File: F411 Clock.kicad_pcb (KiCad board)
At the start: 2 copper layers, 2 parts, among them U1 STM32F411CCUx

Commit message: PCB Save: 1 files changed F411 Clock.kicad_pcb 644/0/0
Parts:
- added J1: USB_C_Receptacle_USB2.0_16P, Connector_USB:USB_C_Receptacle_HCTL_HC-TYPE-C-16P-01A, F.Cu at (108.3, 87.4)
- added R1: R_Small, Resistor_SMD:R_0805_2012Metric, F.Cu at (104.5, 96.0)

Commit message: PCB Save: 1 files changed F411 Clock.kicad_pcb 0/0/2
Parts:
- moved J1 5.73 mm to (106.5, 82.0)
- moved U1 5.73 mm to (124.2, 80.7)
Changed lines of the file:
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@@
 	(footprint "Connector_USB:USB_C_Receptacle_HCTL_HC-TYPE-C-16P-01A"
 		(layer "F.Cu")
-		(at 108.345 87.425)
+		(at 106.5 82)
 		(descr "16-pin USB-C receptacle, USB2.0 and PD, 5A VBUS rating, https://datasheet.lcsc.com/lcsc/2211161000_HCTL-HC-TYPE-C-16P-01A_C2894897.pdf")
 		(tags "usb usb-c 2.0 pd")
@@
 	(footprint "Package_DFN_QFN:QFN-48-1EP_7x7mm_P0.5mm_EP5.15x5.15mm"
 		(layer "F.Cu")
-		(at 126.065 86.145)
+		(at 124.22 80.72)
 		(descr "QFN, 48 Pin (http://www.analog.com/media/en/package-pcb-resources/package/pkg_pdf/ltc-legacy-qfn/QFN_48_05-08-1704.pdf)")
 		(tags "QFN NoLead")

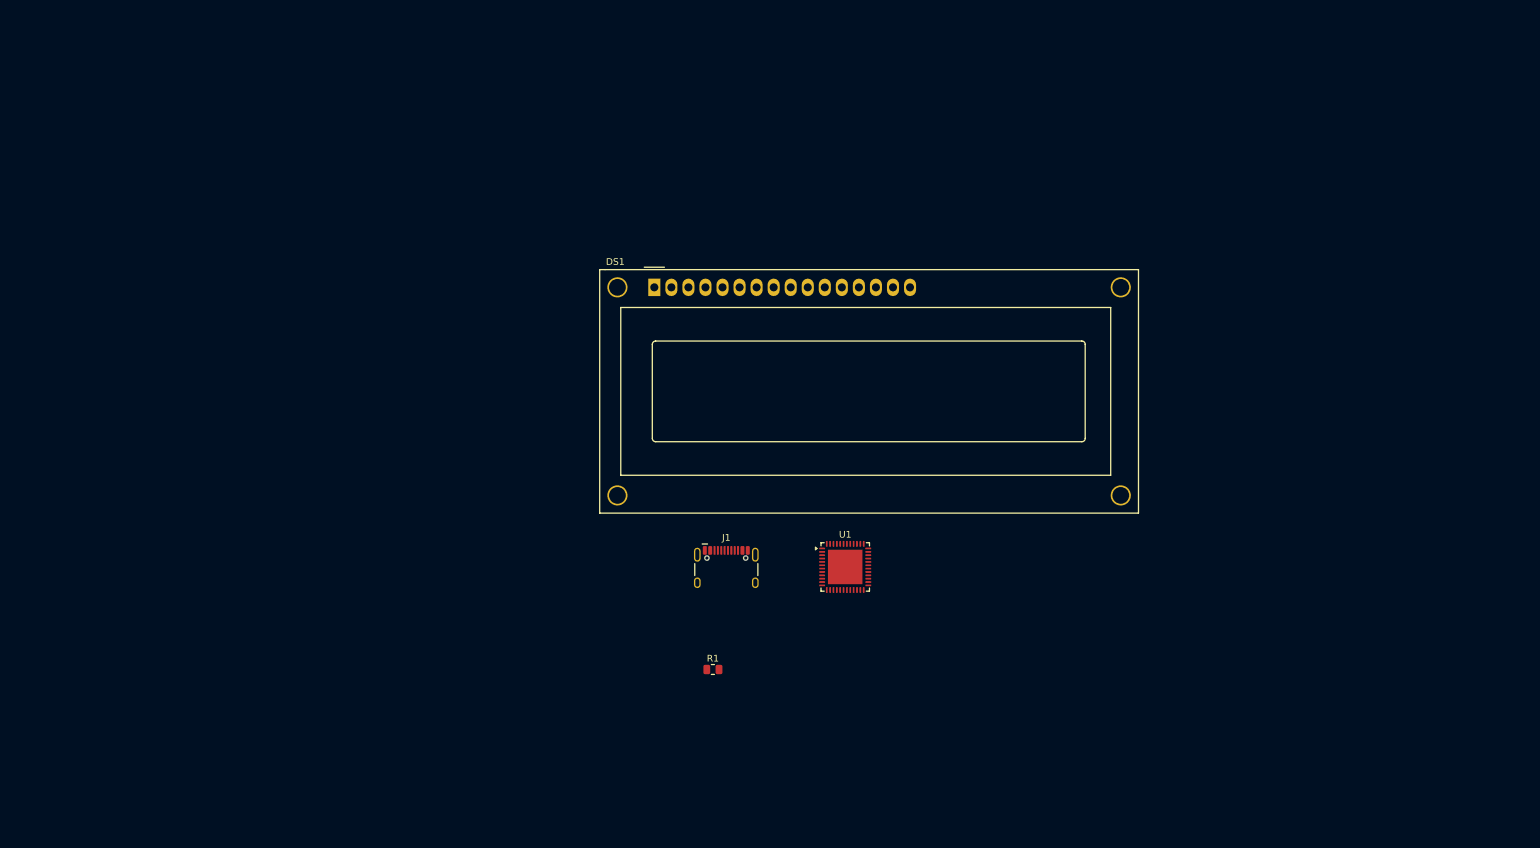
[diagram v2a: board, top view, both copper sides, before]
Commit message: Add .gitignore and update PCB footprints; remove unused files
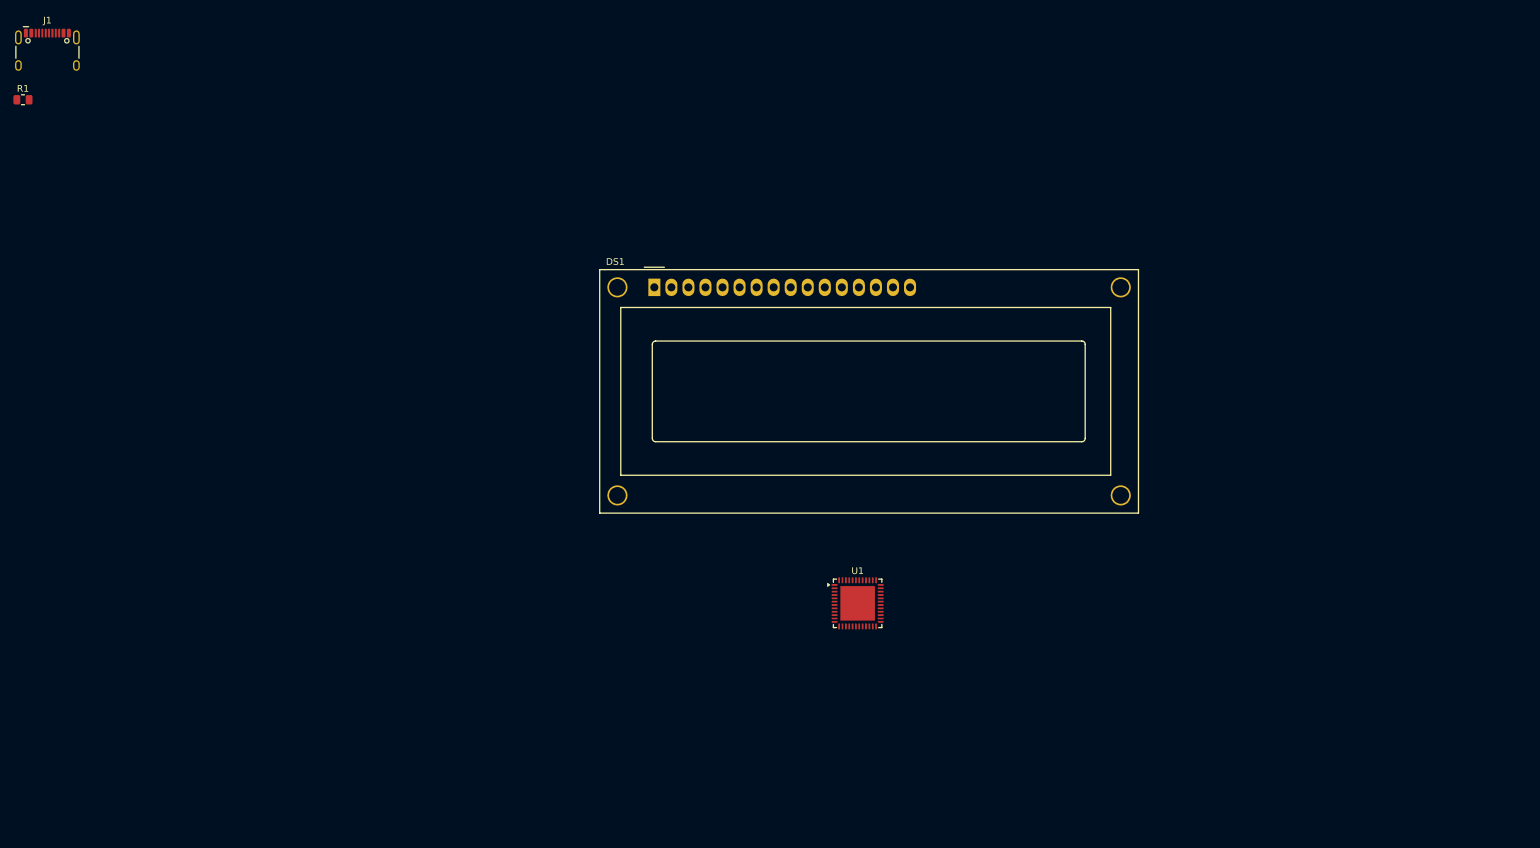
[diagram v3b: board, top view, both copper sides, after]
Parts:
- moved R1 133.3 mm to (1.71, 11.1)
- moved J1 127.2 mm to (5.34, 4.92)
- moved U1 5.73 mm to (126.1, 86.1)
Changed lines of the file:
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@@
 	(footprint "Connector_USB:USB_C_Receptacle_HCTL_HC-TYPE-C-16P-01A"
 		(layer "F.Cu")
-		(at 106.5 82)
+		(at 5.345 4.925)
 		(descr "16-pin USB-C receptacle, USB2.0 and PD, 5A VBUS rating, https://datasheet.lcsc.com/lcsc/2211161000_HCTL-HC-TYPE-C-16P-01A_C2894897.pdf")
 		(tags "usb usb-c 2.0 pd")
@@
 	(footprint "Resistor_SMD:R_0805_2012Metric"
 		(layer "F.Cu")
-		(at 104.5 96)
+		(at 1.705 11.105)
 		(descr "Resistor SMD 0805 (2012 Metric), square (rectangular) end terminal, IPC-7351 nominal, (Body size source: IPC-SM-782 page 72, https://www.pcb-3d.com/wordpress/wp-content/uploads/ipc-sm-782a_amendment_1_and_2.pdf)")
 		(tags "resistor")
@@
 	(footprint "Package_DFN_QFN:QFN-48-1EP_7x7mm_P0.5mm_EP5.15x5.15mm"
 		(layer "F.Cu")
-		(at 124.22 80.72)
+		(at 126.065 86.145)
 		(descr "QFN, 48 Pin (http://www.analog.com/media/en/package-pcb-resources/package/pkg_pdf/ltc-legacy-qfn/QFN_48_05-08-1704.pdf)")
 		(tags "QFN NoLead")

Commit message: Close: 3 files changed F411 Clock.kicad_pcb 0/0/3 F411 Clock.kicad_prl 138/0/0 F411 Clock.kicad_pro 651/0/0
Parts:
- moved R1 133.3 mm to (104.5, 96.0)
- moved J1 127.2 mm to (106.5, 82.0)
- moved U1 5.73 mm to (124.2, 80.7)
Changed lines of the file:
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@@
 	(footprint "Connector_USB:USB_C_Receptacle_HCTL_HC-TYPE-C-16P-01A"
 		(layer "F.Cu")
-		(at 5.345 4.925)
+		(at 106.5 82)
 		(descr "16-pin USB-C receptacle, USB2.0 and PD, 5A VBUS rating, https://datasheet.lcsc.com/lcsc/2211161000_HCTL-HC-TYPE-C-16P-01A_C2894897.pdf")
 		(tags "usb usb-c 2.0 pd")
@@
 	(footprint "Resistor_SMD:R_0805_2012Metric"
 		(layer "F.Cu")
-		(at 1.705 11.105)
+		(at 104.5 96)
 		(descr "Resistor SMD 0805 (2012 Metric), square (rectangular) end terminal, IPC-7351 nominal, (Body size source: IPC-SM-782 page 72, https://www.pcb-3d.com/wordpress/wp-content/uploads/ipc-sm-782a_amendment_1_and_2.pdf)")
 		(tags "resistor")
@@
 	(footprint "Package_DFN_QFN:QFN-48-1EP_7x7mm_P0.5mm_EP5.15x5.15mm"
 		(layer "F.Cu")
-		(at 126.065 86.145)
+		(at 124.22 80.72)
 		(descr "QFN, 48 Pin (http://www.analog.com/media/en/package-pcb-resources/package/pkg_pdf/ltc-legacy-qfn/QFN_48_05-08-1704.pdf)")
 		(tags "QFN NoLead")

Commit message: PCB Save: 2 files changed F411 Clock.kicad_pcb 6362/0/1538 ~F411 Clock.kicad_pcb.lck 1/0/0
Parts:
- added BT1: Battery, Battery:BatteryHolder_MPD_BK-18650-PC2, B.Cu at (163.9, 54.0)
- added BT2: Battery_Cell, Battery:BatteryHolder_Keystone_3034_1x20mm, F.Cu at (195.9, 111.1)
- added C1: 10uf, Capacitor_SMD:C_0805_2012Metric, F.Cu at (210.6, 101.5)
- added C2: 10uf, Capacitor_SMD:C_0805_2012Metric, F.Cu at (210.6, 104.5)
- added C3: 10uf, Capacitor_SMD:C_0805_2012Metric, F.Cu at (210.6, 107.6)
- added C4: 10uf, Capacitor_SMD:C_0805_2012Metric, F.Cu at (210.6, 110.6)
- added C5: 10uf, Capacitor_SMD:C_0805_2012Metric, F.Cu at (210.6, 113.6)
- added D1: 1N5819, Diode_SMD:D_0805_2012Metric, F.Cu at (223.9, 106.0)
- added Q1: DMG3415U, Package_TO_SOT_SMD:SOT-23, F.Cu at (224.1, 102.3)
- added Q2: BC547, Package_TO_SOT_THT:TO-92L_Wide, F.Cu at (214.3, 118.9)
- added R10: 10k, Resistor_SMD:R_0805_2012Metric, F.Cu at (219.4, 110.4)
- added R11: 10k, Resistor_SMD:R_0805_2012Metric, F.Cu at (219.4, 113.3)
- added R2: 10k, Resistor_SMD:R_0805_2012Metric, F.Cu at (215.0, 101.5)
- added R3: 5.2k, Resistor_SMD:R_0805_2012Metric, F.Cu at (215.0, 104.5)
- added R4: 5.2k, Resistor_SMD:R_0805_2012Metric, F.Cu at (215.0, 107.4)
- added R5: 10k, Resistor_SMD:R_0805_2012Metric, F.Cu at (215.0, 110.4)
- added R6: 10k, Resistor_SMD:R_0805_2012Metric, F.Cu at (215.0, 113.3)
- added R7: 10k, Resistor_SMD:R_0805_2012Metric, F.Cu at (219.4, 101.5)
- added R8: 10k, Resistor_SMD:R_0805_2012Metric, F.Cu at (219.4, 104.5)
- added R9: 10k, Resistor_SMD:R_0805_2012Metric, F.Cu at (219.4, 107.4)
- added SW1: SW_Push, Button_Switch_SMD:SW_SPST_TL3342, B.Cu at (121.1, 67.5)
- added SW2: SW_Push, Button_Switch_SMD:SW_SPST_TL3342, B.Cu at (114.0, 67.5)
- added SW3: SW_Push, Button_Switch_SMD:SW_SPST_TL3342, B.Cu at (107.0, 67.5)
- added SW4: SW_Push, Button_Switch_SMD:SW_SPST_TL3342, B.Cu at (100.0, 67.5)
- J1: footprint Connector_USB:USB_C_Receptacle_HCTL_HC-TYPE-C-16P-01A -> Connector_USB:USB_C_Receptacle_GCT_USB4105-xx-A_16P_TopMnt_Horizontal
- R1: value R_Small -> 10k
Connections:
- DS1 pad 1: unconnected-(DS1-VSS-Pad1) -> GND
- DS1 pad 15: unconnected-(DS1-LED(+)-Pad15) -> +3.3V
- DS1 pad 16: unconnected-(DS1-LED(-)-Pad16) -> Net-(DS1-LED(-))
- DS1 pad 2: unconnected-(DS1-VDD-Pad2) -> VBUS
- J1 pad A1: Net-(J1-GND-PadA1) -> GND
- J1 pad A12: Net-(J1-GND-PadA1) -> GND
- J1 pad A5: unconnected-(J1-CC1-PadA5) -> Net-(J1-CC1)
- J1 pad B1: Net-(J1-GND-PadA1) -> GND
- J1 pad B12: Net-(J1-GND-PadA1) -> GND
- J1 pad B5: unconnected-(J1-CC2-PadB5) -> Net-(J1-CC2)
- J1 pad SH: unconnected-(J1-SHIELD-PadSH) -> GND
- R1 pad 1: unconnected-(R1-Pad1) -> /DN
- R1 pad 2: unconnected-(R1-Pad2) -> Net-(J1-D--PadA7)
- U1 pad 1: unconnected-(U1-VBAT-Pad1) -> +BATT_2
- U1 pad 23: Net-(U1-VSS-Pad23) -> GND
- U1 pad 24: unconnected-(U1-VDD-Pad24) -> +3.3V
- U1 pad 32: unconnected-(U1-PA11-Pad32) -> /DN
- U1 pad 33: unconnected-(U1-PA12-Pad33) -> /DP
- U1 pad 35: Net-(U1-VSS-Pad23) -> GND
- U1 pad 36: unconnected-(U1-VDD-Pad36) -> +3.3V
- U1 pad 44: unconnected-(U1-BOOT0-Pad44) -> Net-(U1-BOOT0)
- U1 pad 47: Net-(U1-VSS-Pad23) -> GND
- U1 pad 48: unconnected-(U1-VDD-Pad48) -> +3.3V
- U1 pad 49: Net-(U1-VSS-Pad23) -> GND
- U1 pad 7: unconnected-(U1-NRST-Pad7) -> Net-(U1-NRST)
- U1 pad 8: unconnected-(U1-VSSA-Pad8) -> GND
- U1 pad 9: unconnected-(U1-VDDA-Pad9) -> +3.3AV

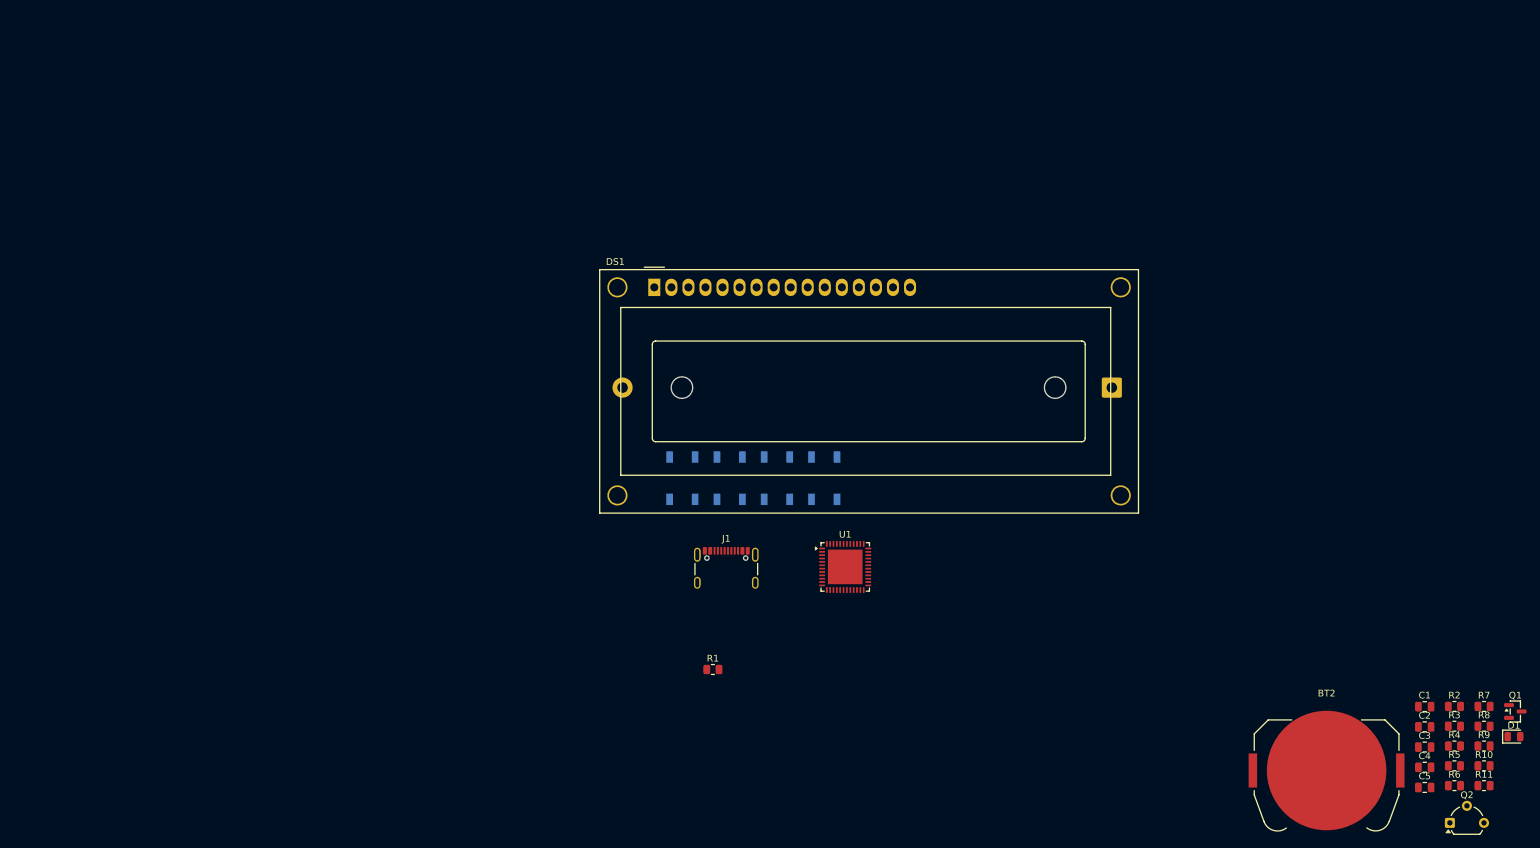
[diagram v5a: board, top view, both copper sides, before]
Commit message: Batter Holder and Buttons
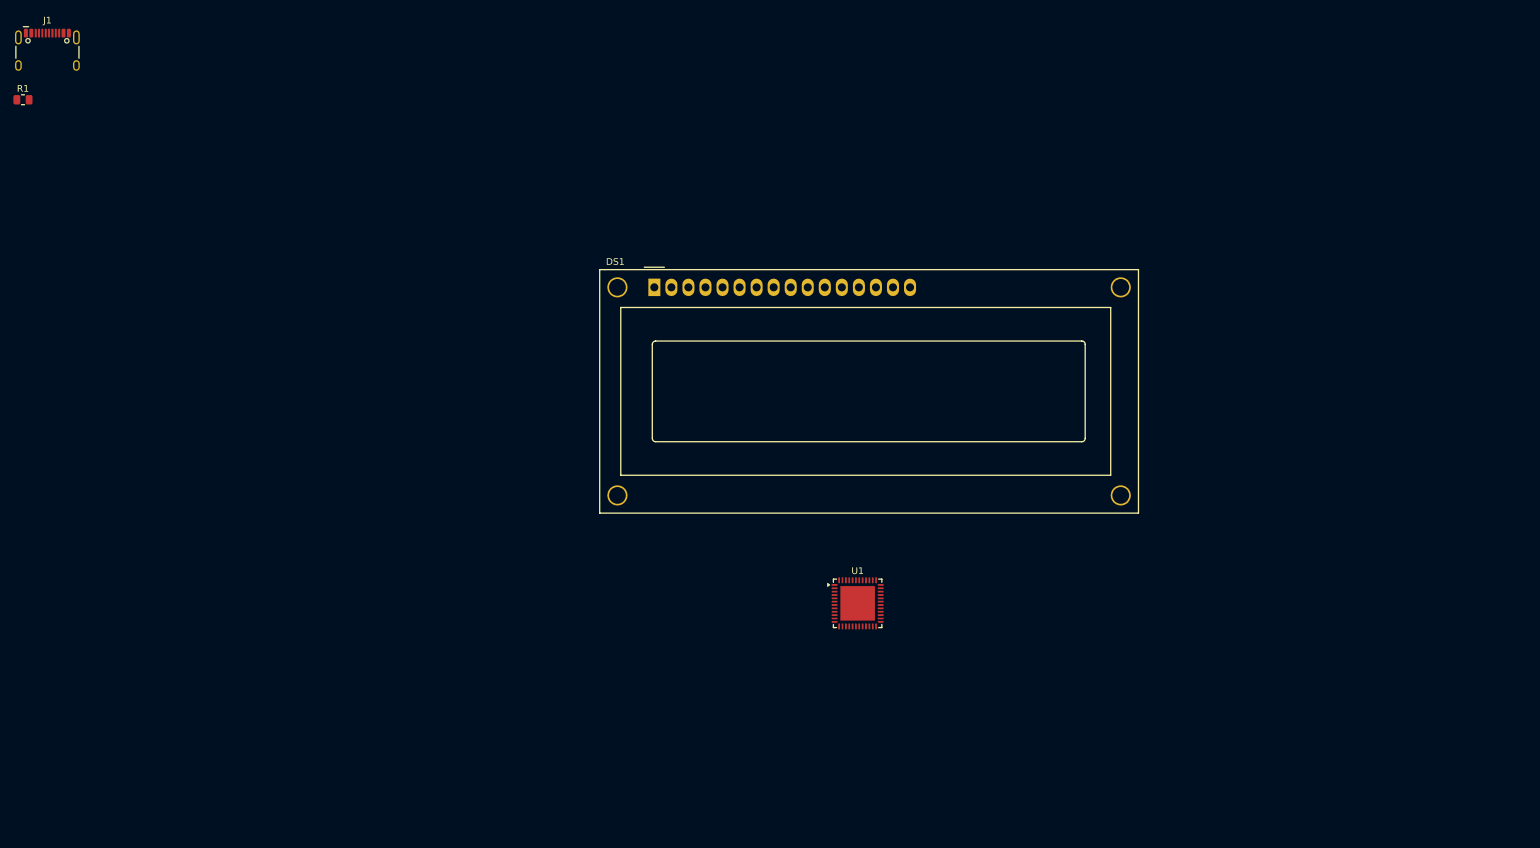
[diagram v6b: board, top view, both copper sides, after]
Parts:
- removed BT1: Battery, Battery:BatteryHolder_MPD_BK-18650-PC2
- removed BT2: Battery_Cell, Battery:BatteryHolder_Keystone_3034_1x20mm
- removed C1, C2, C3, C4, C5: 10uf, Capacitor_SMD:C_0805_2012Metric
- removed D1: 1N5819, Diode_SMD:D_0805_2012Metric
- removed Q1: DMG3415U, Package_TO_SOT_SMD:SOT-23
- removed Q2: BC547, Package_TO_SOT_THT:TO-92L_Wide
- removed R10, R11, R2, R5, R6, R7, R8, R9: 10k, Resistor_SMD:R_0805_2012Metric
- removed R3, R4: 5.2k, Resistor_SMD:R_0805_2012Metric
- removed SW1, SW2, SW3, SW4: SW_Push, Button_Switch_SMD:SW_SPST_TL3342
- J1: footprint Connector_USB:USB_C_Receptacle_GCT_USB4105-xx-A_16P_TopMnt_Horizontal -> Connector_USB:USB_C_Receptacle_HCTL_HC-TYPE-C-16P-01A
- R1: value 10k -> R_Small
- moved R1 133.3 mm to (1.71, 11.1)
- moved J1 127.2 mm to (5.34, 4.92)
- moved U1 5.73 mm to (126.1, 86.1)
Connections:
- DS1 pad 1: GND -> unconnected-(DS1-VSS-Pad1)
- DS1 pad 15: +3.3V -> unconnected-(DS1-LED(+)-Pad15)
- DS1 pad 16: Net-(DS1-LED(-)) -> unconnected-(DS1-LED(-)-Pad16)
- DS1 pad 2: VBUS -> unconnected-(DS1-VDD-Pad2)
- J1 pad A1: GND -> Net-(J1-GND-PadA1)
- J1 pad A12: GND -> Net-(J1-GND-PadA1)
- J1 pad A5: Net-(J1-CC1) -> unconnected-(J1-CC1-PadA5)
- J1 pad B1: GND -> Net-(J1-GND-PadA1)
- J1 pad B12: GND -> Net-(J1-GND-PadA1)
- J1 pad B5: Net-(J1-CC2) -> unconnected-(J1-CC2-PadB5)
- J1 pad SH: GND -> unconnected-(J1-SHIELD-PadSH)
- R1 pad 1: /DN -> unconnected-(R1-Pad1)
- R1 pad 2: Net-(J1-D--PadA7) -> unconnected-(R1-Pad2)
- U1 pad 1: +BATT_2 -> unconnected-(U1-VBAT-Pad1)
- U1 pad 23: GND -> Net-(U1-VSS-Pad23)
- U1 pad 24: +3.3V -> unconnected-(U1-VDD-Pad24)
- U1 pad 32: /DN -> unconnected-(U1-PA11-Pad32)
- U1 pad 33: /DP -> unconnected-(U1-PA12-Pad33)
- U1 pad 35: GND -> Net-(U1-VSS-Pad23)
- U1 pad 36: +3.3V -> unconnected-(U1-VDD-Pad36)
- U1 pad 44: Net-(U1-BOOT0) -> unconnected-(U1-BOOT0-Pad44)
- U1 pad 47: GND -> Net-(U1-VSS-Pad23)
- U1 pad 48: +3.3V -> unconnected-(U1-VDD-Pad48)
- U1 pad 49: GND -> Net-(U1-VSS-Pad23)
- U1 pad 7: Net-(U1-NRST) -> unconnected-(U1-NRST-Pad7)
- U1 pad 8: GND -> unconnected-(U1-VSSA-Pad8)
- U1 pad 9: +3.3AV -> unconnected-(U1-VDDA-Pad9)
